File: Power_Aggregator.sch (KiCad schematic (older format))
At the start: 8 parts, among them P20 XT60, P21 XT60, Q13 AUIRFS8409-7P, Q14 AUIRFS8409-7P, U5 LTC4357, U6 LTC4357

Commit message: Update Netlist
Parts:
- renumbered Q13 to Q7, Q14 to Q8
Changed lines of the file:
@@
 $EndComp
 $Comp
-L AUIRFS8409-7P Q14
+L AUIRFS8409-7P Q8
 U 1 1 5626F582
 P 5200 4100
-F 0 "Q14" H 5210 4270 60  0000 R CNN
+F 0 "Q8" H 5210 4270 60  0000 R CNN
 F 1 "AUIRFS8409-7P" H 5210 3950 60  0000 R CNN
 F 2 "Zeabus:D2PAK-7" H 5200 4100 60  0001 C CNN
@@
 $EndComp
 $Comp
-L GND #PWR042
+L GND #PWR45
 U 1 1 5626F752
 P 6350 5250
-F 0 "#PWR042" H 6350 5000 50  0001 C CNN
+F 0 "#PWR45" H 6350 5000 50  0001 C CNN
 F 1 "GND" H 6350 5100 50  0000 C CNN
 F 2 "" H 6350 5250 60  0000 C CNN
@@
 $EndComp
 $Comp
-L GND #PWR043
+L GND #PWR43
 U 1 1 5626F76E
 P 4050 4600
-F 0 "#PWR043" H 4050 4350 50  0001 C CNN
+F 0 "#PWR43" H 4050 4350 50  0001 C CNN
 F 1 "GND" H 4050 4450 50  0000 C CNN
 F 2 "" H 4050 4600 60  0000 C CNN
@@
 $EndComp
 $Comp
-L AUIRFS8409-7P Q13
+L AUIRFS8409-7P Q7
 U 1 1 5626F953
 P 5200 2200
-F 0 "Q13" H 5210 2370 60  0000 R CNN
+F 0 "Q7" H 5210 2370 60  0000 R CNN
 F 1 "AUIRFS8409-7P" H 5210 2050 60  0000 R CNN
 F 2 "Zeabus:D2PAK-7" H 5200 2200 60  0001 C CNN
@@
 $EndComp
 $Comp
-L GND #PWR044
+L GND #PWR44
 U 1 1 5626F959
 P 6350 3350
-F 0 "#PWR044" H 6350 3100 50  0001 C CNN
+F 0 "#PWR44" H 6350 3100 50  0001 C CNN
 F 1 "GND" H 6350 3200 50  0000 C CNN
 F 2 "" H 6350 3350 60  0000 C CNN
@@
 $EndComp
 $Comp
-L GND #PWR045
+L GND #PWR42
 U 1 1 5626F95F
 P 4050 2700
-F 0 "#PWR045" H 4050 2450 50  0001 C CNN
+F 0 "#PWR42" H 4050 2450 50  0001 C CNN
 F 1 "GND" H 4050 2550 50  0000 C CNN
 F 2 "" H 4050 2700 60  0000 C CNN

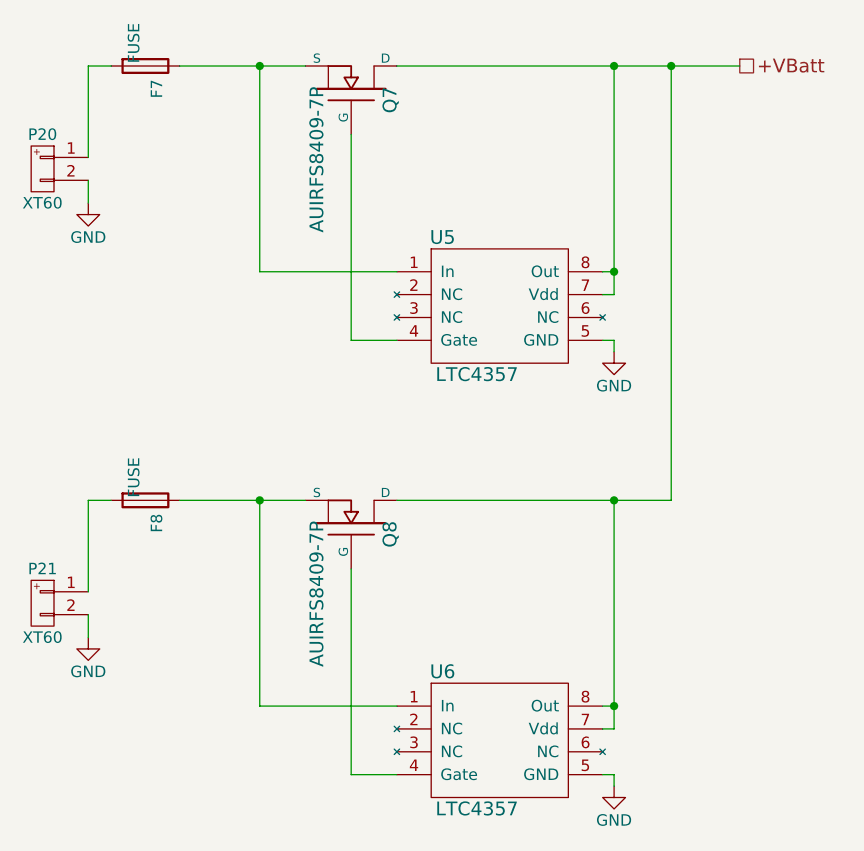
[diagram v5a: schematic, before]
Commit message: Correct GND mixed-up and re-route USB signals as a differential pairs with match length.
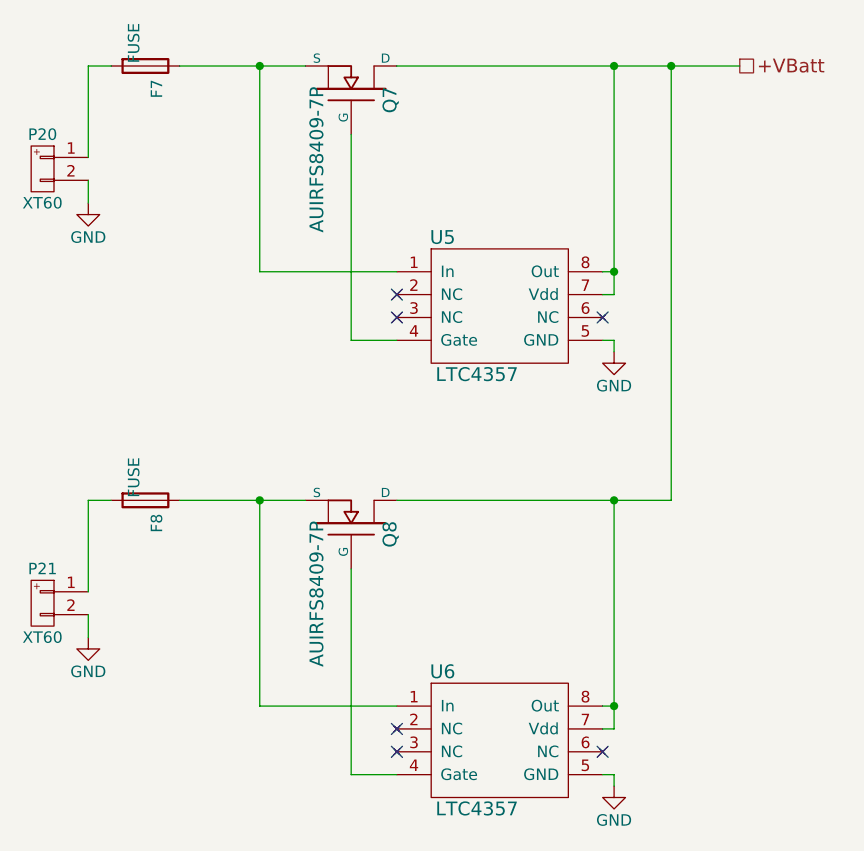
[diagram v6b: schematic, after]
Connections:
- no-connect marks 0 -> 6
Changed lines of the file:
@@
 $Descr A4 11693 8268
 encoding utf-8
-Sheet 9 9
+Sheet 8 9
 Title "Power Aggregator"
 Date "2017-04-06"
@@
 $EndComp
 $Comp
-L GND #PWR45
+L GND #PWR040
 U 1 1 5626F752
 P 6350 5250
-F 0 "#PWR45" H 6350 5000 50  0001 C CNN
+F 0 "#PWR040" H 6350 5000 50  0001 C CNN
 F 1 "GND" H 6350 5100 50  0000 C CNN
 F 2 "" H 6350 5250 60  0000 C CNN
@@
 $EndComp
 $Comp
-L GND #PWR43
+L GND #PWR041
 U 1 1 5626F76E
 P 4050 4600
-F 0 "#PWR43" H 4050 4350 50  0001 C CNN
+F 0 "#PWR041" H 4050 4350 50  0001 C CNN
 F 1 "GND" H 4050 4450 50  0000 C CNN
 F 2 "" H 4050 4600 60  0000 C CNN
@@
 $EndComp
 $Comp
-L GND #PWR44
+L GND #PWR042
 U 1 1 5626F959
 P 6350 3350
-F 0 "#PWR44" H 6350 3100 50  0001 C CNN
+F 0 "#PWR042" H 6350 3100 50  0001 C CNN
 F 1 "GND" H 6350 3200 50  0000 C CNN
 F 2 "" H 6350 3350 60  0000 C CNN
@@
 $EndComp
 $Comp
-L GND #PWR42
+L GND #PWR043
 U 1 1 5626F95F
 P 4050 2700
-F 0 "#PWR42" H 4050 2450 50  0001 C CNN
+F 0 "#PWR043" H 4050 2450 50  0001 C CNN
 F 1 "GND" H 4050 2550 50  0000 C CNN
 F 2 "" H 4050 2700 60  0000 C CNN
@@
 Wire Wire Line
 	4050 4000 4150 4000
+NoConn ~ 6300 5100
+NoConn ~ 5400 5000
+NoConn ~ 5400 5100
+NoConn ~ 5400 3100
+NoConn ~ 5400 3200
+NoConn ~ 6300 3200
 $EndSCHEMATC

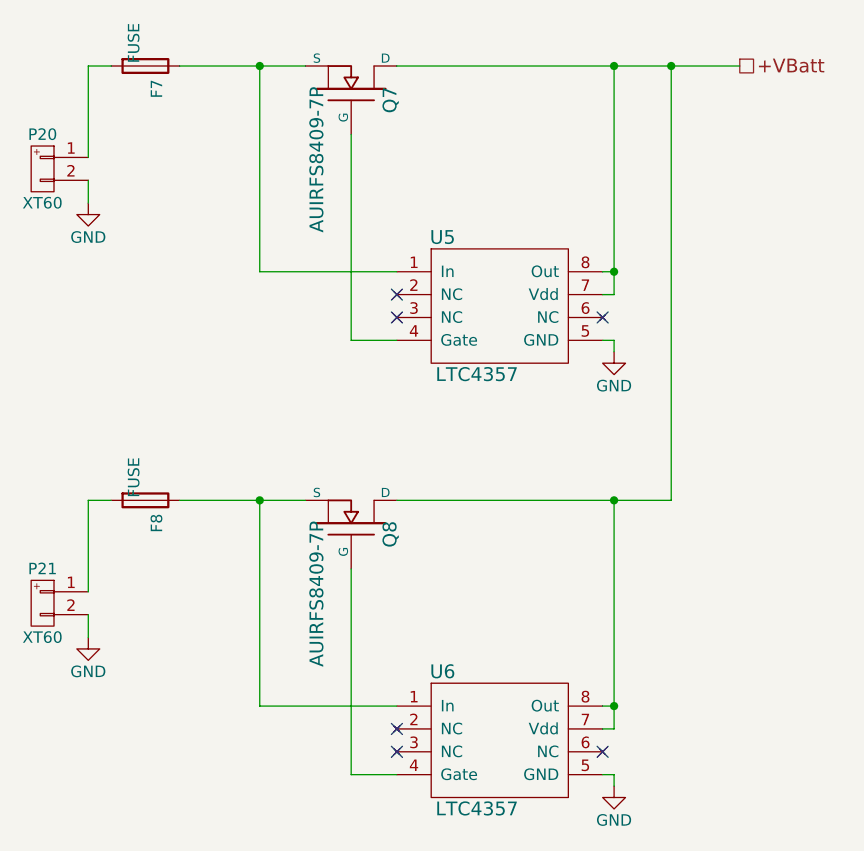
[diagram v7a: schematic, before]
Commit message: change circuit for i6a negative logic on/off
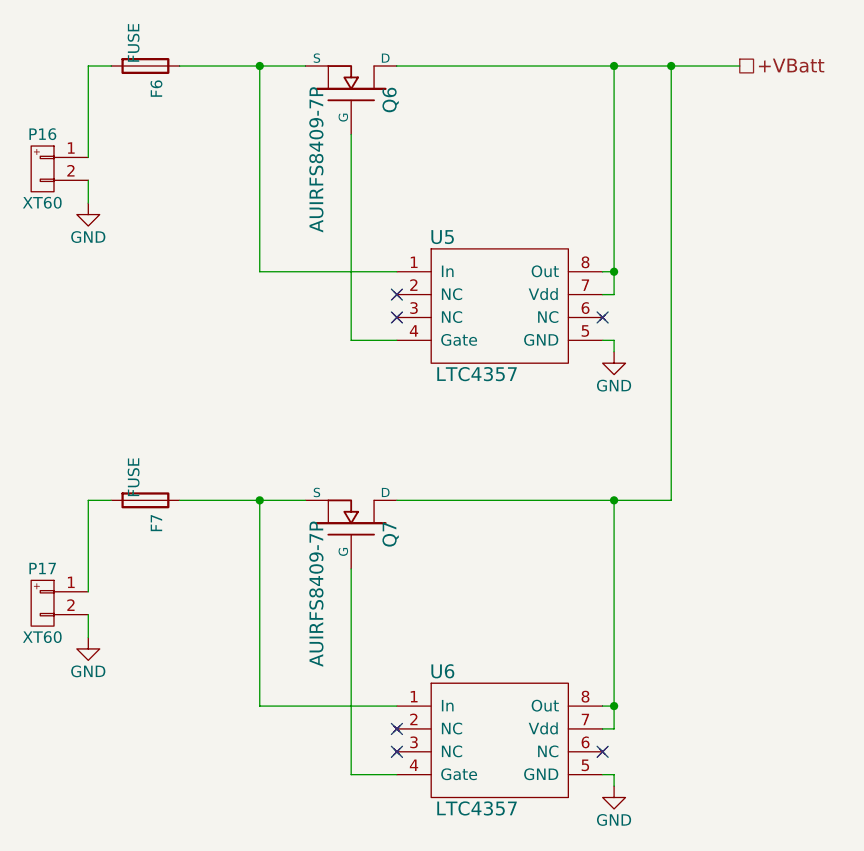
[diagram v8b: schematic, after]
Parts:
- renumbered F7 to F6, F8 to F7, P20 to P16, P21 to P17, Q7 to Q6, Q8 to Q7
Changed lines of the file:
@@
 LIBS:zeabus
 LIBS:ftdi
+LIBS:Power_Distributor-cache
 EELAYER 25 0
 EELAYER END
@@
 $EndDescr
 $Comp
-L Fuse F8
+L Fuse F7
 U 1 1 5626464E
 P 4300 4000
-F 0 "F8" H 4400 4050 50  0000 C CNN
+F 0 "F7" H 4400 4050 50  0000 C CNN
 F 1 "FUSE" H 4200 3950 50  0000 C CNN
 F 2 "Zeabus:FUSE_AUTO" H 4300 4000 60  0001 C CNN
@@
 $EndComp
 $Comp
-L XT60 P21
+L XT60 P17
 U 1 1 5626F4F4
 P 3850 4450
-F 0 "P21" H 3850 4600 50  0000 C CNN
+F 0 "P17" H 3850 4600 50  0000 C CNN
 F 1 "XT60" H 3850 4300 50  0000 C CNN
 F 2 "Zeabus:XT60" H 3850 4450 60  0001 C CNN
@@
 $EndComp
 $Comp
-L AUIRFS8409-7P Q8
+L AUIRFS8409-7P Q7
 U 1 1 5626F582
 P 5200 4100
-F 0 "Q8" H 5210 4270 60  0000 R CNN
+F 0 "Q7" H 5210 4270 60  0000 R CNN
 F 1 "AUIRFS8409-7P" H 5210 3950 60  0000 R CNN
 F 2 "Zeabus:D2PAK-7" H 5200 4100 60  0001 C CNN
@@
 	4050 4500 4050 4600
 $Comp
-L Fuse F7
+L Fuse F6
 U 1 1 5626F941
 P 4300 2100
-F 0 "F7" H 4400 2150 50  0000 C CNN
+F 0 "F6" H 4400 2150 50  0000 C CNN
 F 1 "FUSE" H 4200 2050 50  0000 C CNN
 F 2 "Zeabus:FUSE_AUTO" H 4300 2100 60  0001 C CNN
@@
 $EndComp
 $Comp
-L XT60 P20
+L XT60 P16
 U 1 1 5626F947
 P 3850 2550
-F 0 "P20" H 3850 2700 50  0000 C CNN
+F 0 "P16" H 3850 2700 50  0000 C CNN
 F 1 "XT60" H 3850 2400 50  0000 C CNN
 F 2 "Zeabus:XT60" H 3850 2550 60  0001 C CNN
@@
 $EndComp
 $Comp
-L AUIRFS8409-7P Q7
+L AUIRFS8409-7P Q6
 U 1 1 5626F953
 P 5200 2200
-F 0 "Q7" H 5210 2370 60  0000 R CNN
+F 0 "Q6" H 5210 2370 60  0000 R CNN
 F 1 "AUIRFS8409-7P" H 5210 2050 60  0000 R CNN
 F 2 "Zeabus:D2PAK-7" H 5200 2200 60  0001 C CNN
